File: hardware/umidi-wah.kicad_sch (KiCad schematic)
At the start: 33 parts, among them J1 Conn_01x02, J10 Conn_02x05_Odd_Even, J2 Conn_01x02, J3 Conn_02x05_Odd_Even, J4 Conn_01x02, J5 Input, J6 Output, J7 Conn_02x05_Odd_Even, J8 Conn_02x05_Odd_Even, J9 Conn_02x05_Odd_Even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

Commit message: Fix Opamps
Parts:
- D3: footprint (none) -> LED_THT:LED_D5.0mm
- J1, J2: footprint (none) -> Connector_Wire:SolderWire-1sqmm_1x02_P5.4mm_D1.4mm_OD2.7mm
- J4: footprint (none) -> Connector_Wire:SolderWire-1sqmm_1x02_P5.4mm_D1.4mm_OD2.7mm; Function (none) -> Bypass toggle
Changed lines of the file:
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@@
   )
   (symbol (lib_id "Connector_Generic:Conn_01x02") (at 179.07 157.48 0) (unit 1)
-    (in_bom yes) (on_board yes) (dnp no) (fields_autoplaced)
+    (in_bom yes) (on_board yes) (dnp no)
     (property "Reference" "J4" (at 179.07 151.13 0)
       (effects (font (size 1.27 1.27)))
@@
       (effects (font (size 1.27 1.27)))
     )
-    (property "Footprint" "" (at 179.07 157.48 0)
+    (property "Footprint" "Connector_Wire:SolderWire-1sqmm_1x02_P5.4mm_D1.4mm_OD2.7mm" (at 179.07 157.48 0)
       (effects (font (size 1.27 1.27)) hide)
     )
     (property "Datasheet" "~" (at 179.07 157.48 0)
       (effects (font (size 1.27 1.27)) hide)
+    )
+    (property "Function" "Bypass toggle" (at 182.118 163.83 0)
+      (effects (font (size 1.27 1.27)))
     )
     (pin "1")
@@
       (effects (font (size 1.27 1.27)))
     )
-    (property "Footprint" "" (at 26.67 25.4 0)
+    (property "Footprint" "Connector_Wire:SolderWire-1sqmm_1x02_P5.4mm_D1.4mm_OD2.7mm" (at 26.67 25.4 0)
       (effects (font (size 1.27 1.27)) hide)
     )
@@
       (effects (font (size 1.27 1.27)))
     )
-    (property "Footprint" "" (at 104.14 25.4 0)
+    (property "Footprint" "Connector_Wire:SolderWire-1sqmm_1x02_P5.4mm_D1.4mm_OD2.7mm" (at 104.14 25.4 0)
       (effects (font (size 1.27 1.27)) hide)
     )
@@
       (effects (font (size 1.27 1.27)) (justify right))
     )
-    (property "Footprint" "" (at 161.29 171.45 0)
-      (effects (font (size 1.27 1.27)) hide)
-    )
+    (property "Footprint" "LED_THT:LED_D5.0mm" (at 161.29 171.45 0)
+      (effects (font (size 1.27 1.27)) hide)
+    )

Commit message: Assign all footprints
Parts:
- C10, C11, C18, C4: footprint (none) -> Capacitor_SMD:C_1206_3216Metric_Pad1.33x1.80mm_HandSolder
- C19, C21, C5, C9: footprint (none) -> Capacitor_SMD:C_0805_2012Metric_Pad1.18x1.45mm_HandSolder
- R24, R25, R28, R29, R31, R32, R35, R8, R9: footprint (none) -> Resistor_SMD:R_0805_2012Metric_Pad1.20x1.40mm_HandSolder
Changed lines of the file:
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@@
       (effects (font (size 1.27 1.27)) (justify left))
     )
-    (property "Footprint" "" (at 230.632 95.25 90)
+    (property "Footprint" "Resistor_SMD:R_0805_2012Metric_Pad1.20x1.40mm_HandSolder" (at 230.632 95.25 90)
       (effects (font (size 1.27 1.27)) hide)
     )
@@
       (effects (font (size 1.27 1.27)) (justify left))
     )
-    (property "Footprint" "" (at 82.2452 34.29 0)
+    (property "Footprint" "Capacitor_SMD:C_0805_2012Metric_Pad1.18x1.45mm_HandSolder" (at 82.2452 34.29 0)
       (effects (font (size 1.27 1.27)) hide)
     )
@@
       (effects (font (size 1.27 1.27)) (justify left))
     )
-    (property "Footprint" "" (at 60.6552 34.29 0)
+    (property "Footprint" "Capacitor_SMD:C_0805_2012Metric_Pad1.18x1.45mm_HandSolder" (at 60.6552 34.29 0)
       (effects (font (size 1.27 1.27)) hide)
     )
@@
       (effects (font (size 1.27 1.27)) (justify right))
     )
-    (property "Footprint" "" (at 86.868 65.405 90)
+    (property "Footprint" "Resistor_SMD:R_0805_2012Metric_Pad1.20x1.40mm_HandSolder" (at 86.868 65.405 90)
       (effects (font (size 1.27 1.27)) hide)
     )
@@
       (effects (font (size 1.27 1.27)) (justify left))
     )
-    (property "Footprint" "" (at 232.1052 137.16 0)
+    (property "Footprint" "Capacitor_SMD:C_0805_2012Metric_Pad1.18x1.45mm_HandSolder" (at 232.1052 137.16 0)
       (effects (font (size 1.27 1.27)) hide)
     )
@@
       (effects (font (size 1.27 1.27)) (justify right))
     )
-    (property "Footprint" "" (at 163.068 163.83 90)
+    (property "Footprint" "Resistor_SMD:R_0805_2012Metric_Pad1.20x1.40mm_HandSolder" (at 163.068 163.83 90)
       (effects (font (size 1.27 1.27)) hide)
     )
@@
       (effects (font (size 1.27 1.27)))
     )
-    (property "Footprint" "" (at 245.11 150.622 90)
+    (property "Footprint" "Resistor_SMD:R_0805_2012Metric_Pad1.20x1.40mm_HandSolder" (at 245.11 150.622 90)
       (effects (font (size 1.27 1.27)) hide)
     )
@@
       (effects (font (size 1.27 1.27)) (justify right))
     )
-    (property "Footprint" "" (at 168.148 152.4 90)
+    (property "Footprint" "Resistor_SMD:R_0805_2012Metric_Pad1.20x1.40mm_HandSolder" (at 168.148 152.4 90)
       (effects (font (size 1.27 1.27)) hide)
     )
@@
       (effects (font (size 1.27 1.27)) (justify left))
     )
-    (property "Footprint" "" (at 88.5952 34.29 0)
+    (property "Footprint" "Capacitor_SMD:C_1206_3216Metric_Pad1.33x1.80mm_HandSolder" (at 88.5952 34.29 0)
       (effects (font (size 1.27 1.27)) hide)
     )
@@
       (effects (font (size 1.27 1.27)) (justify left))
     )
-    (property "Footprint" "" (at 94.9452 69.85 0)
+    (property "Footprint" "Capacitor_SMD:C_1206_3216Metric_Pad1.33x1.80mm_HandSolder" (at 94.9452 69.85 0)
       (effects (font (size 1.27 1.27)) hide)
     )
@@
       (effects (font (size 1.27 1.27)) (justify left))
     )
-    (property "Footprint" "" (at 217.932 95.25 90)
+    (property "Footprint" "Resistor_SMD:R_0805_2012Metric_Pad1.20x1.40mm_HandSolder" (at 217.932 95.25 90)
       (effects (font (size 1.27 1.27)) hide)
     )
@@
       (effects (font (size 1.27 1.27)) (justify left))
     )
-    (property "Footprint" "" (at 218.1352 137.16 0)
+    (property "Footprint" "Capacitor_SMD:C_0805_2012Metric_Pad1.18x1.45mm_HandSolder" (at 218.1352 137.16 0)
       (effects (font (size 1.27 1.27)) hide)
     )
@@
       (effects (font (size 1.27 1.27)) (justify left))
     )
-    (property "Footprint" "" (at 209.2452 137.16 0)
+    (property "Footprint" "Capacitor_SMD:C_1206_3216Metric_Pad1.33x1.80mm_HandSolder" (at 209.2452 137.16 0)
       (effects (font (size 1.27 1.27)) hide)
     )
@@
       (effects (font (size 1.27 1.27)))
     )
-    (property "Footprint" "" (at 224.155 125.222 90)
+    (property "Footprint" "Resistor_SMD:R_0805_2012Metric_Pad1.20x1.40mm_HandSolder" (at 224.155 125.222 90)
       (effects (font (size 1.27 1.27)) hide)
     )
@@
       (effects (font (size 1.27 1.27)) (justify left))
     )
-    (property "Footprint" "" (at 50.4952 34.29 0)
+    (property "Footprint" "Capacitor_SMD:C_1206_3216Metric_Pad1.33x1.80mm_HandSolder" (at 50.4952 34.29 0)
       (effects (font (size 1.27 1.27)) hide)
     )
@@
       (effects (font (size 1.27 1.27)) (justify right))
     )
-    (property "Footprint" "" (at 86.868 53.975 90)
+    (property "Footprint" "Resistor_SMD:R_0805_2012Metric_Pad1.20x1.40mm_HandSolder" (at 86.868 53.975 90)
       (effects (font (size 1.27 1.27)) hide)
     )
@@
       (effects (font (size 1.27 1.27)) (justify left))
     )
-    (property "Footprint" "" (at 224.282 95.25 90)
-      (effects (font (size 1.27 1.27)) hide)
-    )
+    (property "Footprint" "Resistor_SMD:R_0805_2012Metric_Pad1.20x1.40mm_HandSolder" (at 224.282 95.25 90)
+      (effects (font (size 1.27 1.27)) hide)
+    )

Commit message: Add pcb outline and test milling layer
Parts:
- J7, J8: footprint Connector_PinSocket_2.54mm:PinSocket_2x05_P2.54mm_Vertical -> Connector_PinHeader_2.54mm:PinHeader_2x05_P2.54mm_Vertical
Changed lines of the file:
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@@
       (effects (font (size 1.27 1.27)))
     )
-    (property "Footprint" "Connector_PinSocket_2.54mm:PinSocket_2x05_P2.54mm_Vertical" (at 31.75 157.48 0)
+    (property "Footprint" "Connector_PinHeader_2.54mm:PinHeader_2x05_P2.54mm_Vertical" (at 31.75 157.48 0)
       (effects (font (size 1.27 1.27)) hide)
     )
@@
       (effects (font (size 1.27 1.27)))
     )
-    (property "Footprint" "Connector_PinSocket_2.54mm:PinSocket_2x05_P2.54mm_Vertical" (at 77.47 157.48 0)
-      (effects (font (size 1.27 1.27)) hide)
-    )
+    (property "Footprint" "Connector_PinHeader_2.54mm:PinHeader_2x05_P2.54mm_Vertical" (at 77.47 157.48 0)
+      (effects (font (size 1.27 1.27)) hide)
+    )

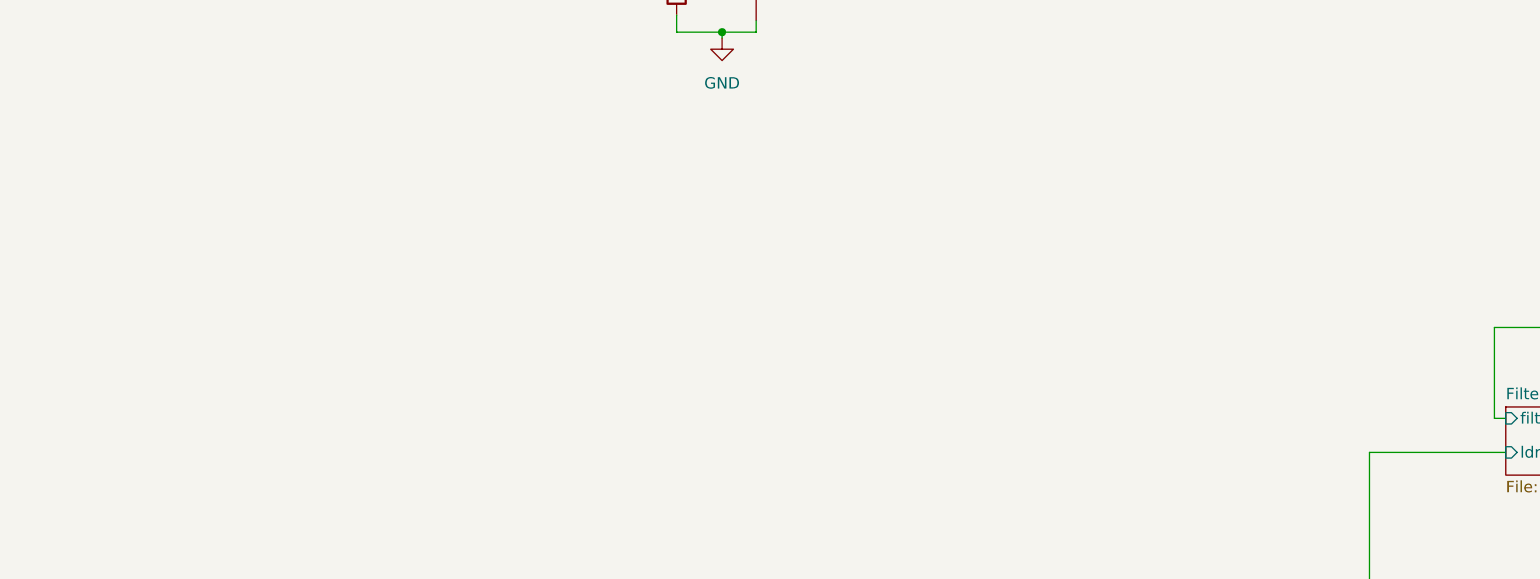
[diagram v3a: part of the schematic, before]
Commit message: Add uMIDI footprint
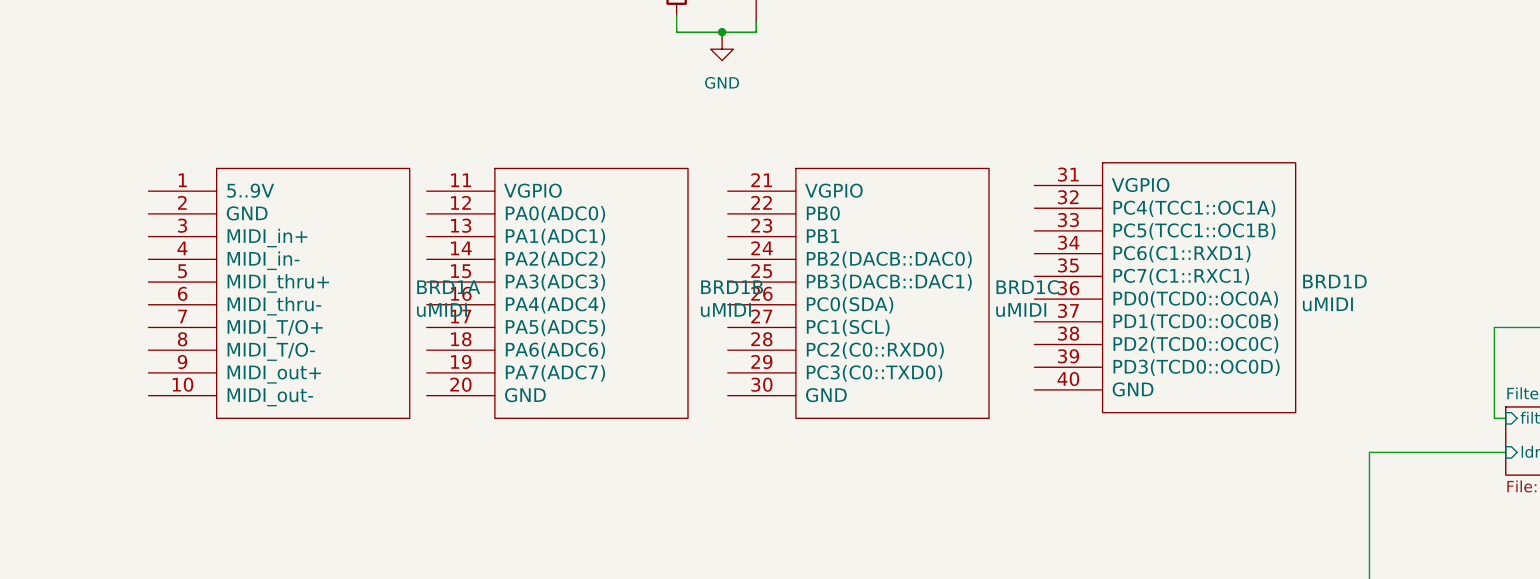
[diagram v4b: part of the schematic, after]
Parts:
- added BRD1: uMIDI, uMidi-wah:uMIDI_faceup, symbol umidi-wah:uMIDI
